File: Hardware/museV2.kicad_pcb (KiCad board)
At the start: 2 copper layers, 142.3 x 55.5 mm, 427 parts, among them P1 RCA_conn_x2, P10 -15V, P11 ~4, P13 ~5, P18 RX7, P19 3.3V, P20 TX6, P21 1.8V, P22 PSU_CTL, P23 GND, P3 3.5mm_conn_tip_switch, P31 P1, P32 L1.8_1, P33 L3.3_1, P34 P2, P35 L1.8_2, P36 L3.3_2, P37 P3, P38 L1.8_3, P39 L3.3_3, P4 3.5mm_conn_tip_switch, P40 P4, P41 L1.8_4, P42 L3.3_4, P43 +5V, P5 CONN_01X06, P6 CONN_02X14, P7 ~2, P8 +15V, P9 ~3, Q1 PMOS, Q2 BSS138, SW1 PWR_BTN, SW2 PAIR_BTN, U1 TPS65130, U10 PCM1863, U11 PCM1796, U12 NE5534, U13 NE5534, U14 NE5534, U15 NE5534, U16 NE5534, U17 NE5534, U18 EdisonConnector, U19 GTL2010, U2 LP38692, U20 GTL2010, U21 GTL2010, U22 PCA9685BS, U3 PLR135/T10, U4 POM-3535L-3-R, U5 POM-3535L-3-R, U6 PLT133/T10W, U7 POM-3535L-3-R, U8 POM-3535L-3-R, U9 PCM9211, X1 24.576 MHz

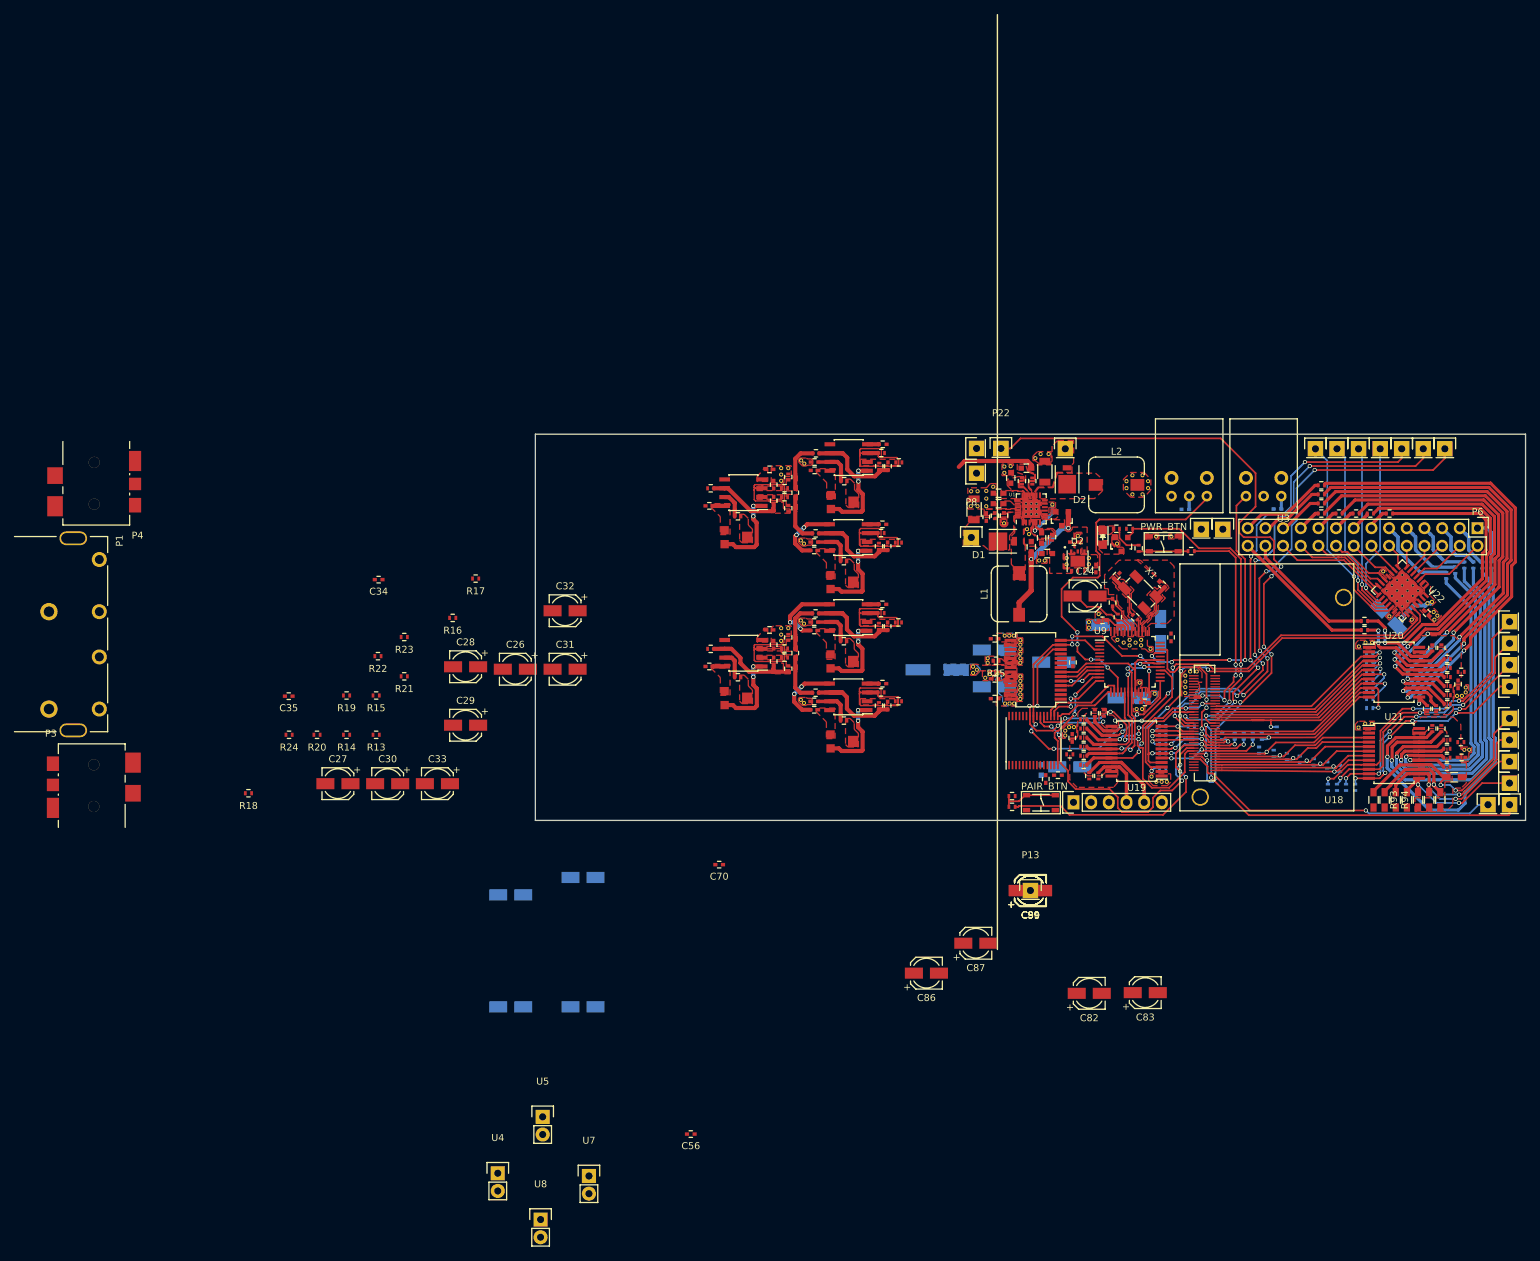
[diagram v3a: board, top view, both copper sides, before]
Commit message: All tracks and planes filled.  Fixing fill intersections and missing power/gnd connections
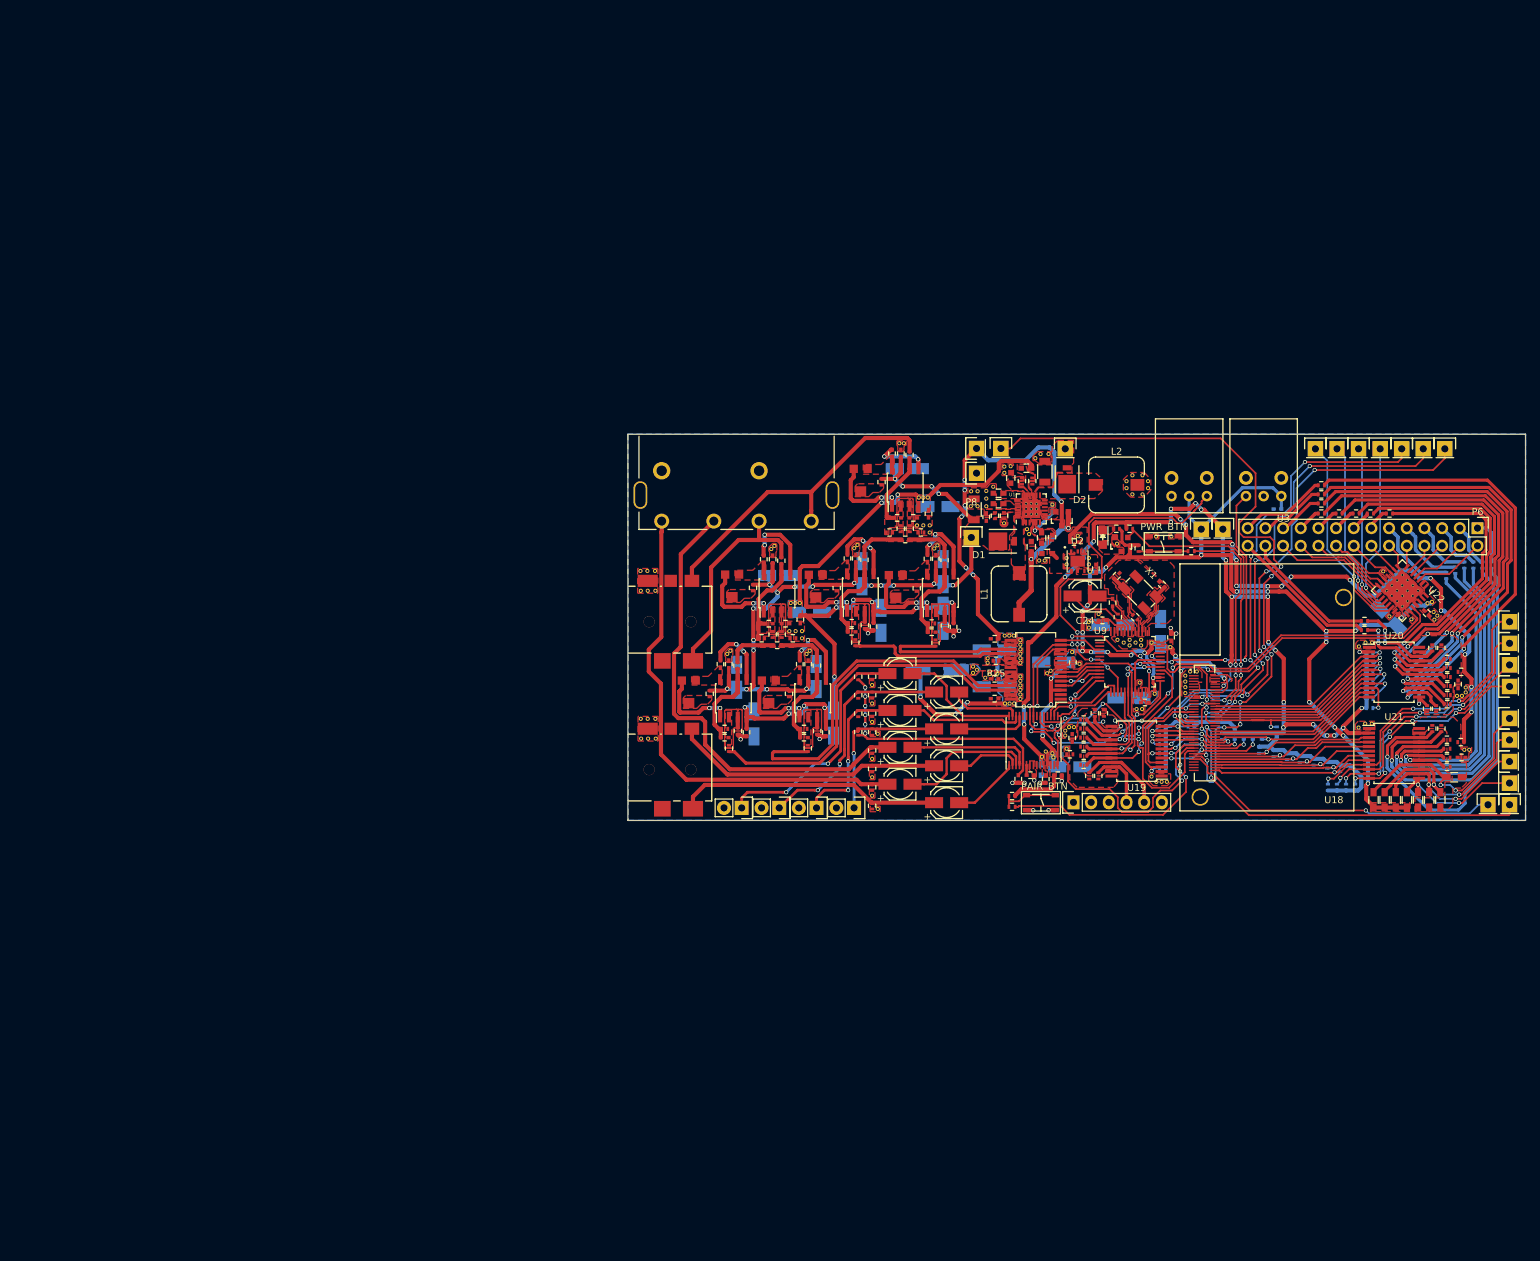
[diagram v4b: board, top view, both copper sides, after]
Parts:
- removed P13: ~5, Pin_Headers:Pin_Header_Straight_1x01
- removed the REF** at (181.6, 126.3)
- added REF**: VIA-0.3mm, muse-v2-lib:VIA-0.3mm, F.Cu at (166.6, 141.1)
- added REF**: VIA-0.3mm, muse-v2-lib:VIA-0.3mm, F.Cu at (108.3, 118.0)
- added REF**: VIA-0.3mm, muse-v2-lib:VIA-0.3mm, F.Cu at (110.4, 115.2)
- added REF**: VIA-0.3mm, muse-v2-lib:VIA-0.3mm, F.Cu at (109.3, 115.2)
- added REF**: VIA-0.3mm, muse-v2-lib:VIA-0.3mm, F.Cu at (108.3, 115.2)
- added REF**: VIA-0.3mm, muse-v2-lib:VIA-0.3mm, F.Cu at (181.8, 125.5)
- added REF**: VIA-0.3mm, muse-v2-lib:VIA-0.3mm, F.Cu at (184.4, 126.1)
- added REF**: VIA-0.3mm, muse-v2-lib:VIA-0.3mm, F.Cu at (166.8, 129.8)
- added REF**: VIA-0.3mm, muse-v2-lib:VIA-0.3mm, F.Cu at (167.2, 129.5)
- added REF**: VIA-0.3mm, muse-v2-lib:VIA-0.3mm, F.Cu at (171.4, 128.5)
- added REF**: VIA-0.3mm, muse-v2-lib:VIA-0.3mm, F.Cu at (170.3, 126.8)
- added REF**: VIA-0.3mm, muse-v2-lib:VIA-0.3mm, F.Cu at (109.3, 136.4)
- added REF**: VIA-0.3mm, muse-v2-lib:VIA-0.3mm, F.Cu at (172.9, 115.2)
- added REF**: VIA-0.3mm, muse-v2-lib:VIA-0.3mm, F.Cu at (142.4, 138.6)
- added REF**: VIA-0.3mm, muse-v2-lib:VIA-0.3mm, F.Cu at (142.4, 149.3)
- added REF**: VIA-0.3mm, muse-v2-lib:VIA-0.3mm, F.Cu at (141.6, 147.4)
- added REF**: VIA-0.3mm, muse-v2-lib:VIA-0.3mm, F.Cu at (141.6, 144.8)
- added REF**: VIA-0.3mm, muse-v2-lib:VIA-0.3mm, F.Cu at (141.6, 142.2)
- added REF**: VIA-0.3mm, muse-v2-lib:VIA-0.3mm, F.Cu at (141.6, 136.8)
- added REF**: VIA-0.3mm, muse-v2-lib:VIA-0.3mm, F.Cu at (141.6, 134.2)
- added REF**: VIA-0.3mm, muse-v2-lib:VIA-0.3mm, F.Cu at (141.6, 131.6)
- added REF**: VIA-0.3mm, muse-v2-lib:VIA-0.3mm, F.Cu at (166.0, 141.8)
- added REF**: VIA-0.3mm, muse-v2-lib:VIA-0.3mm, F.Cu at (110.5, 136.4)
- added REF**: VIA-0.3mm, muse-v2-lib:VIA-0.3mm, F.Cu at (167.5, 141.3)
- added REF**: VIA-0.3mm, muse-v2-lib:VIA-0.3mm, F.Cu at (167.7, 141.9)
- added REF**: VIA-0.3mm, muse-v2-lib:VIA-0.3mm, F.Cu at (169.6, 140.7)
- added REF**: VIA-0.3mm, muse-v2-lib:VIA-0.3mm, F.Cu at (130.6, 119.8)
- added REF**: VIA-0.3mm, muse-v2-lib:VIA-0.3mm, F.Cu at (129.9, 119.8)
- added REF**: VIA-0.3mm, muse-v2-lib:VIA-0.3mm, F.Cu at (131.2, 119.8)
- added REF**: VIA-0.3mm, muse-v2-lib:VIA-0.3mm, F.Cu at (148.9, 104.6)
- added REF**: VIA-0.3mm, muse-v2-lib:VIA-0.3mm, F.Cu at (149.6, 104.6)
- added REF**: VIA-0.3mm, muse-v2-lib:VIA-0.3mm, F.Cu at (148.3, 104.6)
- added REF**: VIA-0.3mm, muse-v2-lib:VIA-0.3mm, F.Cu at (145.5, 96.8)
- added REF**: VIA-0.3mm, muse-v2-lib:VIA-0.3mm, F.Cu at (108.4, 139.2)
- added REF**: VIA-0.3mm, muse-v2-lib:VIA-0.3mm, F.Cu at (146.2, 96.8)
- added REF**: VIA-0.3mm, muse-v2-lib:VIA-0.3mm, F.Cu at (127.1, 112.0)
- added REF**: VIA-0.3mm, muse-v2-lib:VIA-0.3mm, F.Cu at (127.5, 111.5)
- added REF**: VIA-0.3mm, muse-v2-lib:VIA-0.3mm, F.Cu at (108.3, 136.4)
- added REF**: VIA-0.3mm, muse-v2-lib:VIA-0.3mm, F.Cu at (110.5, 139.2)
- added REF**: VIA-0.3mm, muse-v2-lib:VIA-0.3mm, F.Cu at (109.4, 139.2)
- added REF**: VIA-0.3mm, muse-v2-lib:VIA-0.3mm, F.Cu at (110.5, 118.0)
- added REF**: VIA-0.3mm, muse-v2-lib:VIA-0.3mm, F.Cu at (109.3, 118.0)
- C39, C82, C83, C86, C87, C89, C90, C91: moved to B.Cu
- moved C35 107.2 mm to (164.3, 144.5), turned to 0 degrees
- moved P1 102.5 mm to (132.8, 108.0), turned to 180 degrees
- moved C56 102.4 mm to (145.7, 98.3), turned to 90 degrees
- moved C34 96.3 mm to (162.6, 145.1), turned to 270 degrees
- moved R18 90.4 mm to (141.6, 135.7), turned to 270 degrees
- moved P4 83.0 mm to (109.5, 122.5), turned to 0 degrees
- moved R24 82.2 mm to (139.6, 130.3), turned to 270 degrees
- moved C27 80.8 mm to (145.6, 145.8), turned to 0 degrees
- moved R20 80.2 mm to (141.6, 130.3), turned to 270 degrees
- moved P3 80.0 mm to (109.5, 143.7), turned to 0 degrees
- moved C83 79.7 mm to (128.3, 115.8)
- moved C81 76.1 mm to (151.8, 122.0), turned to 90 degrees
- moved R14 75.7 mm to (141.6, 143.6), turned to 270 degrees
- moved R19 75.5 mm to (141.6, 133.0), turned to 270 degrees
- moved C30 75.3 mm to (145.6, 129.9), turned to 0 degrees
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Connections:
- C11 pad 1: +5V -> +5VSB
- C26 pad 1: Net-(C26-Pad1) -> RCA_IN_R
- C26 pad 2: RCA_IN_R -> Net-(C26-Pad2)
- C27 pad 1: Net-(C27-Pad1) -> RCA_IN_L
- C27 pad 2: RCA_IN_L -> Net-(C27-Pad2)
- C28 pad 1: Net-(C28-Pad1) -> 3.5_IN_R
- C28 pad 2: 3.5_IN_R -> Net-(C28-Pad2)
- C29 pad 1: Net-(C29-Pad1) -> 3.5_IN_L
- C29 pad 2: 3.5_IN_L -> Net-(C29-Pad2)
- C30 pad 1: Net-(C30-Pad1) -> MIC_1
- C30 pad 2: MIC_1 -> Net-(C30-Pad2)
- C31 pad 1: Net-(C31-Pad1) -> MIC_2
- C31 pad 2: MIC_2 -> Net-(C31-Pad2)
- C32 pad 1: Net-(C32-Pad1) -> MIC_3
- C32 pad 2: MIC_3 -> Net-(C32-Pad2)
- C33 pad 1: Net-(C33-Pad1) -> MIC_4
- C33 pad 2: MIC_4 -> Net-(C33-Pad2)
- P1 pad 1: RCA_IN_R -> ANALOG_OUT_R
- P1 pad 2: RCA_IN_L -> ANALOG_OUT_L
- P1 pad 3: ANALOG_OUT_R -> RCA_IN_R
- P1 pad 4: ANALOG_OUT_L -> RCA_IN_L
- U10 pad 1: Net-(C29-Pad1) -> Net-(C29-Pad2)
- U10 pad 2: Net-(C28-Pad1) -> Net-(C28-Pad2)
- U10 pad 27: Net-(C33-Pad1) -> Net-(C33-Pad2)
- U10 pad 28: Net-(C32-Pad1) -> Net-(C32-Pad2)
- U10 pad 29: Net-(C31-Pad1) -> Net-(C31-Pad2)
- U10 pad 3: Net-(C27-Pad1) -> Net-(C27-Pad2)
- U10 pad 30: Net-(C30-Pad1) -> Net-(C30-Pad2)
- U10 pad 4: Net-(C26-Pad1) -> Net-(C26-Pad2)
- U2 pad 1: +5V -> +5VSB
- U2 pad 3: +5V -> +5VSB
- U2 pad 6: +5V -> +5VSB
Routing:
- net +1.8VSB: track 0.00 -> 197.2 mm, vias 0 -> 23
- net +3.3VSB: track 28.3 -> 214.2 mm, vias 1 -> 28
- net +5VSB: track 0.00 -> 171.1 mm, vias 0 -> 24
- net -15V: track 18.1 -> 115.7 mm, vias 0 -> 12
- net +15V: track 30.6 -> 109.2 mm, vias 0 -> 21
- net RCA_IN_L: track 0.00 -> 69.3 mm
- net RCA_IN_R: track 0.00 -> 67.3 mm
- net /DAC/sheet57F8A4E6/ANALOG_OUT-: track 0.00 -> 53.4 mm
- net /DAC/sheet57F8A4E6/ANALOG_OUT+: track 0.00 -> 52.4 mm
- net ANALOG_OUT_R: track 0.00 -> 46.8 mm
- net Net-(C34-Pad1): track 0.00 -> 39.0 mm, vias 0 -> 6
- net 3.5_IN_R: track 0.00 -> 38.9 mm
- net 3.5_IN_L: track 0.00 -> 38.1 mm
- net MIC_1: track 0.00 -> 34.9 mm, vias 0 -> 2
- net MIC_2: track 0.00 -> 34.1 mm, vias 0 -> 2
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- added copper zone on F.Cu, net +1.8VSB
- added copper zone on B.Cu, net -15V
- added copper zone on B.Cu, net GND
- removed copper zone on F.Cu, net +5V
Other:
- board size 142.3 x 55.5 mm -> 129 x 55.5 mm

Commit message: Rev 2.0.0 finished.  Ready for design review.
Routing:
- net 3.5_OUT_SEN: track 0.00 -> 110.5 mm, vias 0 -> 2
- net 3.5_IN_SEN: track 0.00 -> 83.0 mm
- net +3.3VSB: track 214.2 -> 217.6 mm, vias 28 -> 31
- net +1.8VSB: track 197.2 -> 199.5 mm, vias 23 -> 24
- net I2S_MCU_DIN(1.8): track 11.7 -> 13.9 mm
- net +5VSB: track 171.1 -> 173.0 mm
- net GND: track 19.8 -> 21.4 mm, vias 14 -> 15
- net MCU_GPIO_X_2/PWM_X_1: track 66.0 -> 64.5 mm
- net MCU_GPIO_X_3/PWM_X_2: track 70.8 -> 69.4 mm
- net MCU_GPIO_X_4/PWM_X_3: track 74.4 -> 73.4 mm
- net LED_IA_10: track 66.0 -> 66.9 mm
- net LED_IA_9: track 67.6 -> 66.8 mm
- net /LIGHT_CONN/LED_B_4: track 17.0 -> 17.7 mm
- net /LIGHT_CONN/LED_B_3: track 10.3 -> 9.69 mm
- net LED_IA_8: track 67.7 -> 67.1 mm
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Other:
- board size 129 x 55.5 mm -> 129 x 55.9 mm
